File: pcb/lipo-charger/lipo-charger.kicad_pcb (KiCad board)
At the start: 2 copper layers, 31 x 24.5 mm, 17 parts, among them J1 USB_B_Micro, J2 BATTERY, J3 OUTPUT, SW1 BATTERY_EN, U1 MCP73831-2-OT

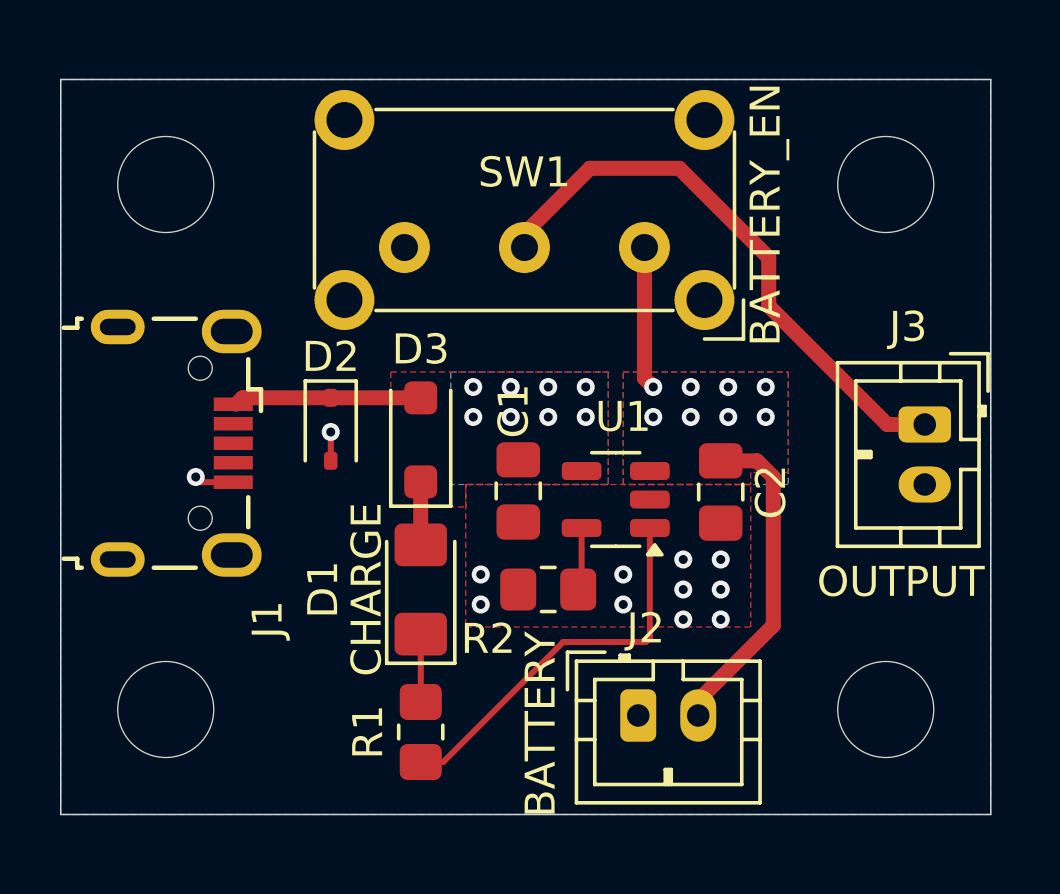
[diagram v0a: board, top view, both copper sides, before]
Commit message: add tooling holes for assembly
https://jlcpcb.com/help/article/47-How-to-add-tooling-holes-for-PCB-assembly-order
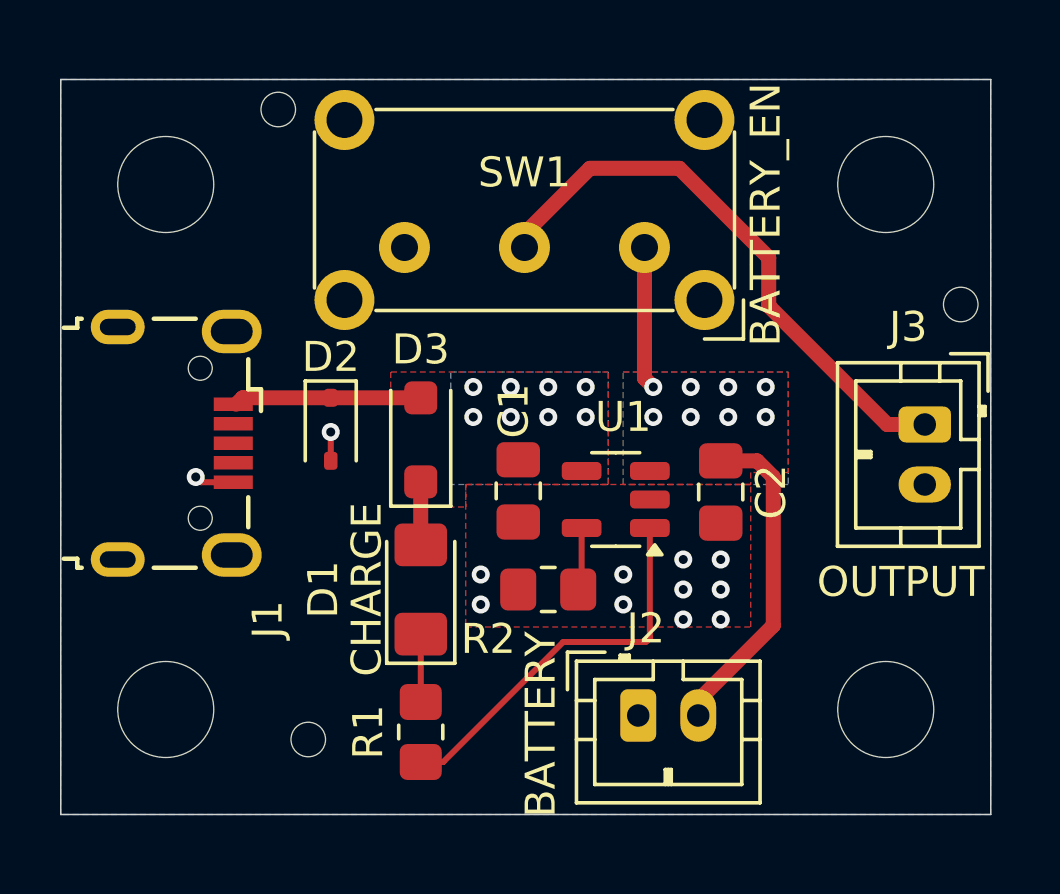
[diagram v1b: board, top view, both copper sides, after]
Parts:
- added REF**: tooling_hole, laser-photogate:tooling_hole, F.Cu at (106.5, 53.0)
- added REF**: tooling_hole, laser-photogate:tooling_hole, F.Cu at (84.8, 67.5)
- added REF**: tooling_hole, laser-photogate:tooling_hole, F.Cu at (83.8, 46.5)

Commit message: remove tooling holes; finalize for production
It's easier to have JLC add the tooling holes.
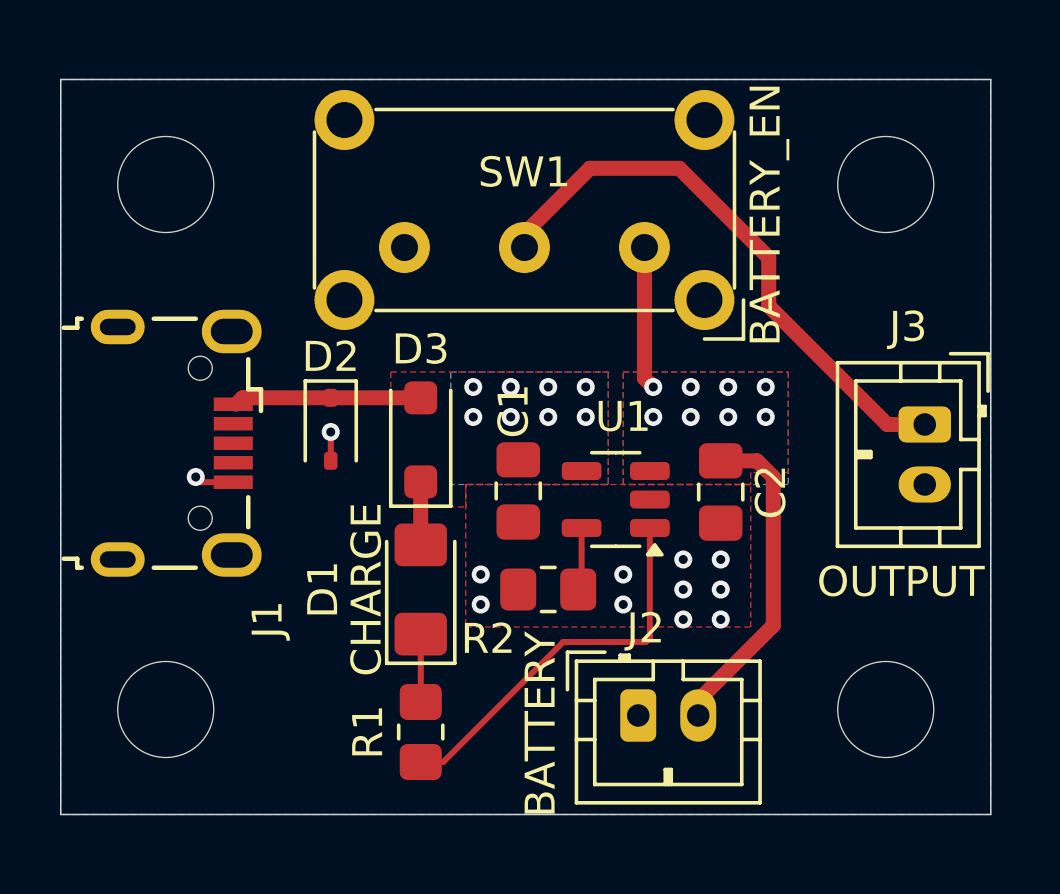
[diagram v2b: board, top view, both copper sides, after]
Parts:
- removed the REF** at (106.5, 53.0)
- removed the REF** at (84.8, 67.5)
- removed the REF** at (83.8, 46.5)
